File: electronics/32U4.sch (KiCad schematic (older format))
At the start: 10 parts, among them J1 Input 5v, U1 Pro Micro 32U4 USB

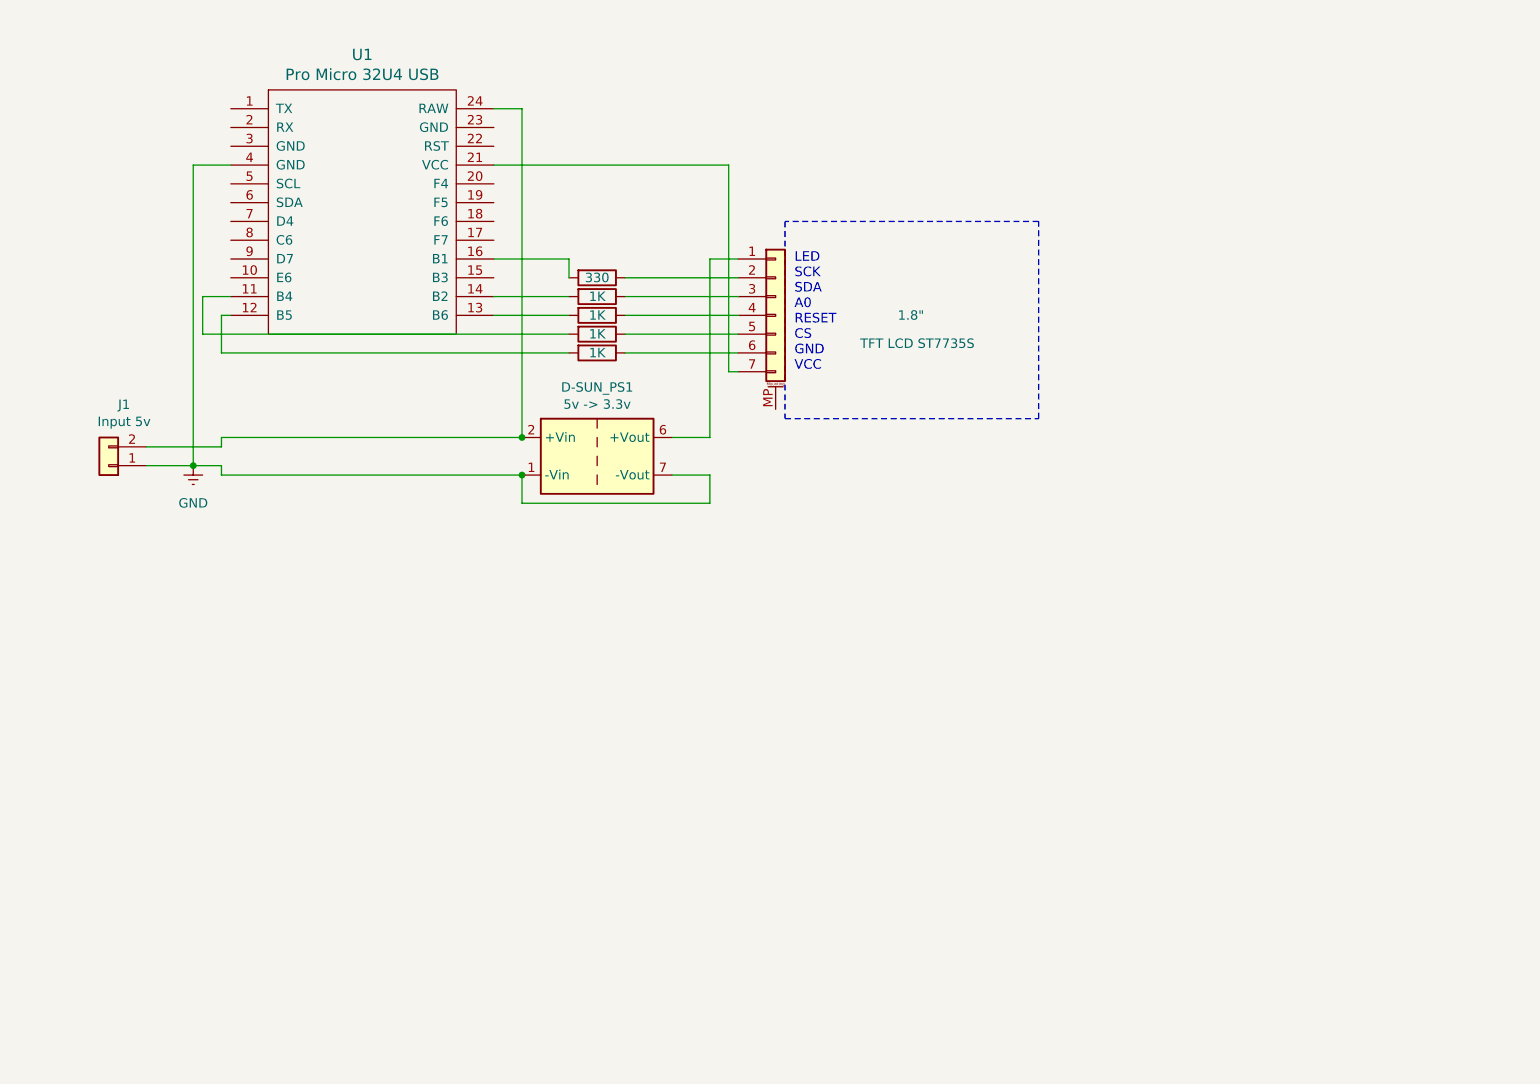
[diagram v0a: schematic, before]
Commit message: Added rotary encoder
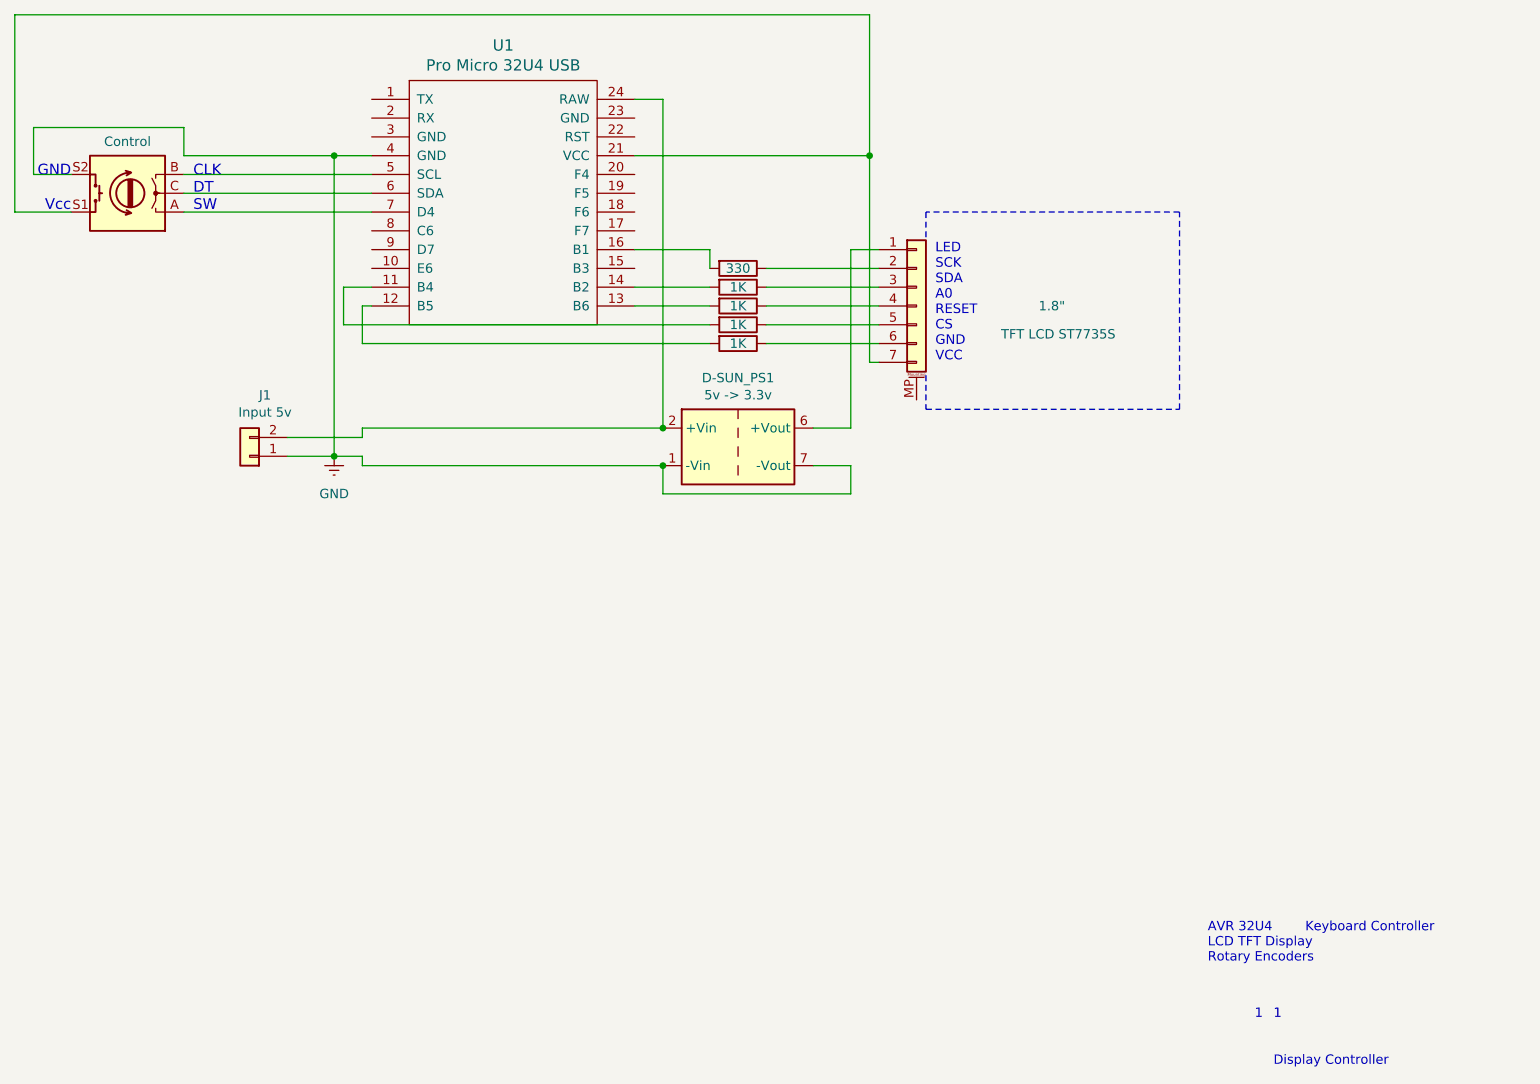
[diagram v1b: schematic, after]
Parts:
- added Control: Rotary_Encoder_Switch, symbol Device:Rotary_Encoder_Switch
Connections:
- net GNDREF: now also Control.S2
- net at 1.8".7 (Pin_7), U1.21 (VCC): now also Control.S1
- net at U1.5 (SCL): now also Control.B
- net at U1.6 (SDA): now also Control.C
- net at U1.7 (D4): now also Control.A
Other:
- note added: "1"
- note added: "AVR 32U4 Keyboard Controller\nLCD TFT Display\nRotary Encoders"
- note added: "CLK\nDT\nSW"
- note added: "Display Controller"
- note added: "GND\n\nVcc"
- moved on the sheet: 1.8", D-SUN_PS1, J1, U1
